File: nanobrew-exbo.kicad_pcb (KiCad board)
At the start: 2 copper layers, 65 x 56.5 mm, 16 parts, among them J1 RPi_GPIO, J2 DS18B20, J3 driver_terminal, J4 driver_terminal, J5 PWR IN 1, J6 PI POWER, J7 PWR IN 2, J8 adc_terminal, U1 ULN2803A, U2 ULN2803A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

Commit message: Adding capacitor
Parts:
- added C1: C_Small, Capacitor_THT:CP_Radial_D4.0mm_P2.00mm, F.Cu at (96.0, 74.0)
- J2: value DS18B20 -> DS18B20 sensors
- R1: value 4K7 -> 3K3
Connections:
- J6 pad 1: +5V -> Net-(C1-Pad1)
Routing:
- net Net-(C1-Pad1): track 0.00 -> 8.39 mm
- net +3V3: track 23.9 -> 31.9 mm
- net GPIO04: track 43.4 -> 39.0 mm
- net +5V: track 32.4 -> 28.3 mm

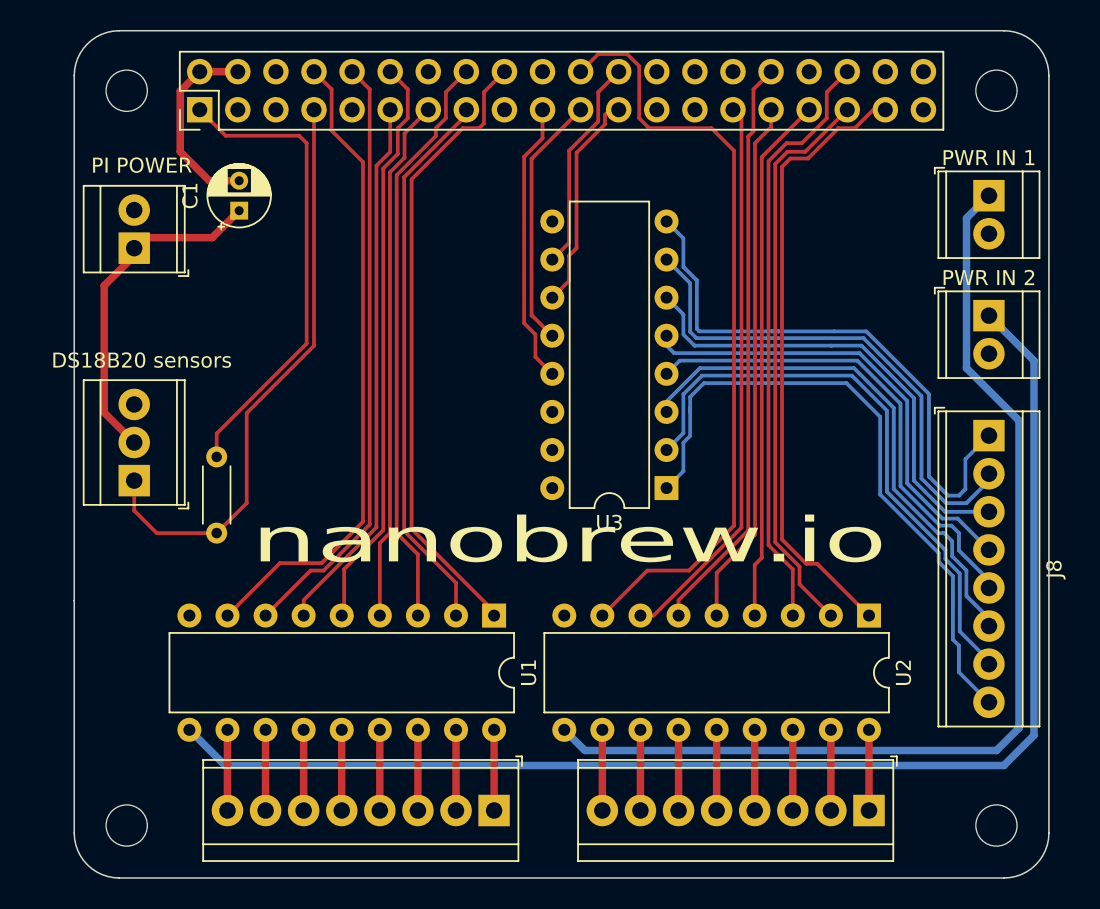
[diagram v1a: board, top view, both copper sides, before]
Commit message: Adding a ground plane.
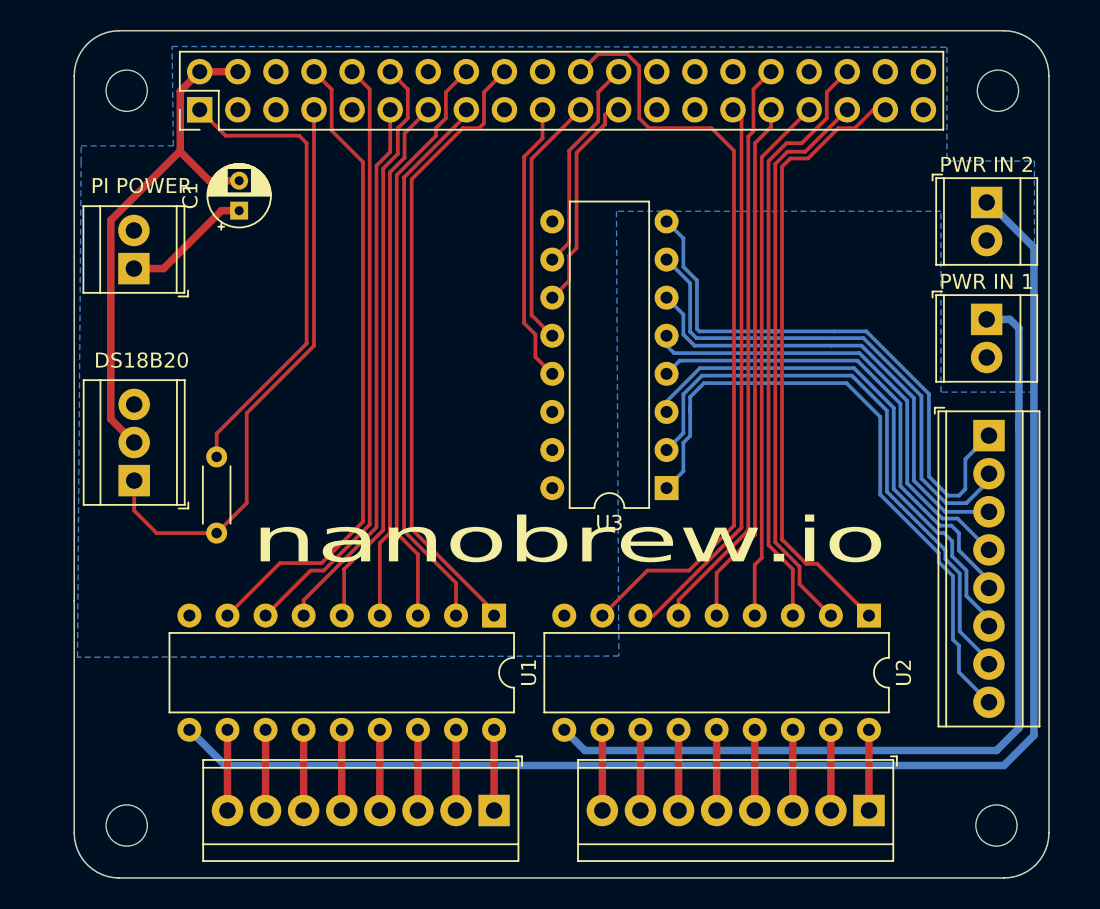
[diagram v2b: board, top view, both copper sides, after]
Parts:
- J2: value DS18B20 sensors -> DS18B20
- moved J5 8.25 mm to (145.8, 81.2)
- moved J7 7.55 mm to (145.8, 73.5)
- moved J6 1.36 mm to (89.0, 77.9)
- moved ? 0.10 mm to (146.6, 66.0)
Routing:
- net PWR1: track 69.1 -> 61.2 mm
- net PWR2: track 87.4 -> 95.1 mm
- net +5V: track 28.3 -> 35.1 mm
- added copper zone on B.Cu, net GND
